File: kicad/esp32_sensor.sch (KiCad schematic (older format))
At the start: 0 parts

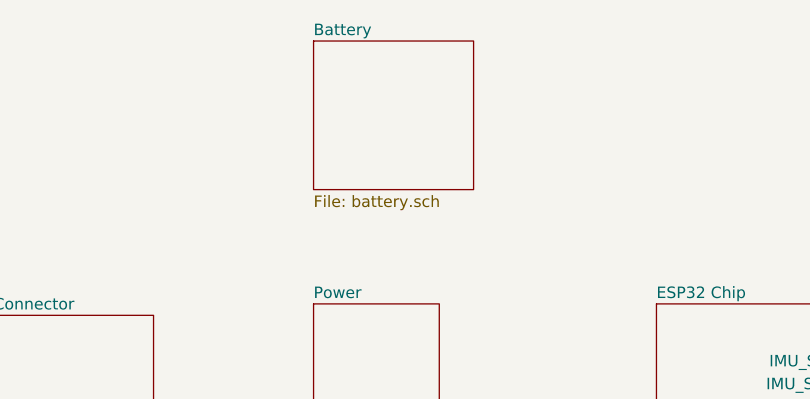
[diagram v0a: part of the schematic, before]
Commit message: Deleted a header pin. Started working on PCB
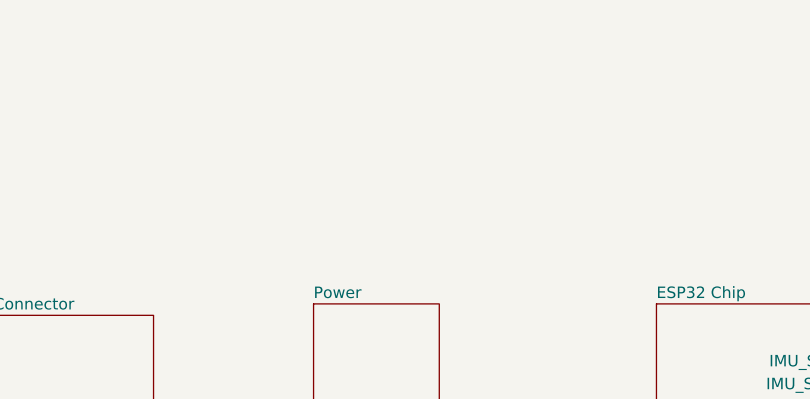
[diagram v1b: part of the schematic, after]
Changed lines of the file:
@@
 $Descr USLetter 11000 8500
 encoding utf-8
-Sheet 1 6
+Sheet 1 5
 Title "ESP32 Sensor Module"
 Date "2020-11-23"
@@
 	6500 3450 5800 3450
 $Sheet
-S 3450 1300 700  650
-U 5FE12D18
-F0 "Battery" 50
-F1 "battery.sch" 50
-$EndSheet
-$Sheet
 S 2050 2500 700  1200

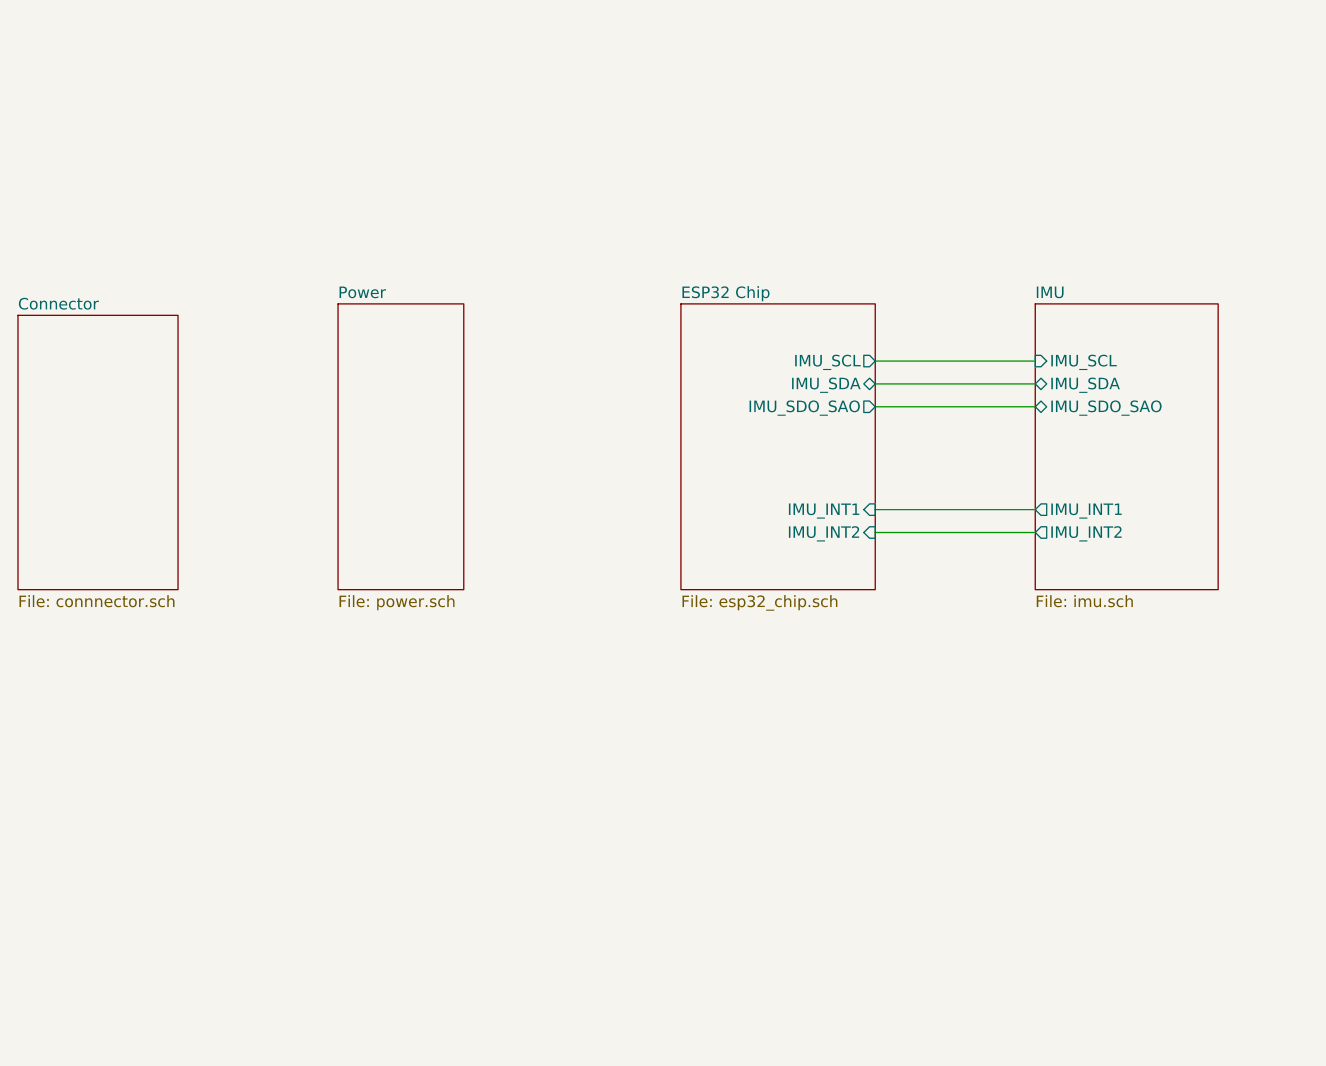
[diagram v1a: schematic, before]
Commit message: Updated schematic and PCB design to v0.0.2 for 2-layer pcb. Added more silkscreen text
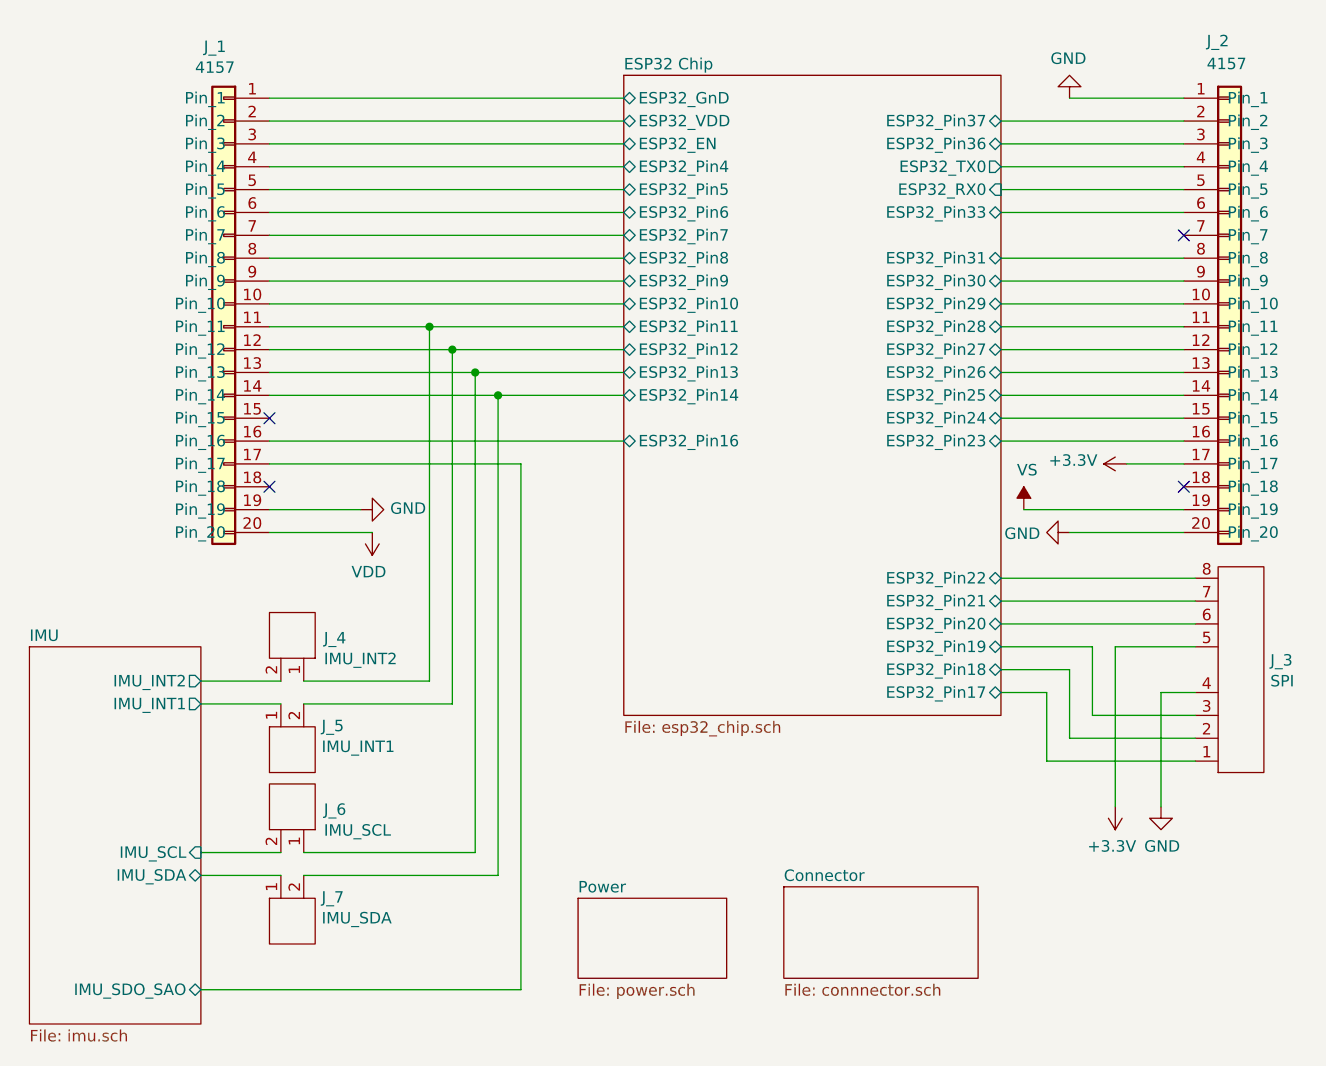
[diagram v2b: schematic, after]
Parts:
- added J_1, J_2: 4157, Connector_PinSocket_2.54mm:PinSocket_1x20_P2.54mm_Vertical, symbol CANtech:4157
- added J_3: SPI, Connector_PinHeader_2.54mm:PinHeader_1x08_P2.54mm_Vertical, symbol CANtech:Header_Pin_8
- added J_4: IMU_INT2, Connector_PinHeader_2.54mm:PinHeader_1x02_P2.54mm_Vertical, symbol CANtech:Header_Pin_2
- added J_5: IMU_INT1, Connector_PinHeader_2.54mm:PinHeader_1x02_P2.54mm_Vertical, symbol CANtech:Header_Pin_2
- added J_6: IMU_SCL, Connector_PinHeader_2.54mm:PinHeader_1x02_P2.54mm_Vertical, symbol CANtech:Header_Pin_2
- added J_7: IMU_SDA, Connector_PinHeader_2.54mm:PinHeader_1x02_P2.54mm_Vertical, symbol CANtech:Header_Pin_2
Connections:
- new net +3V3: J_2.17 (Pin_17), J_3.5
- new net ESP32 Chip/ESP32_EN: J_1.3 (Pin_3)
- new net ESP32 Chip/ESP32_GnD: J_1.1 (Pin_1)
- new net ESP32 Chip/ESP32_Pin10: J_1.10 (Pin_10)
- new net ESP32 Chip/ESP32_Pin11: J_1.11 (Pin_11), J_4.1
- new net ESP32 Chip/ESP32_Pin12: J_1.12 (Pin_12), J_5.2
- new net ESP32 Chip/ESP32_Pin13: J_1.13 (Pin_13), J_6.1
- new net ESP32 Chip/ESP32_Pin14: J_1.14 (Pin_14), J_7.2
- new net ESP32 Chip/ESP32_Pin16: J_1.16 (Pin_16)
- new net ESP32 Chip/ESP32_Pin17: J_3.1
- new net ESP32 Chip/ESP32_Pin18: J_3.2
- new net ESP32 Chip/ESP32_Pin19: J_3.3
- new net ESP32 Chip/ESP32_Pin20: J_3.6
- new net ESP32 Chip/ESP32_Pin21: J_3.7
- new net ESP32 Chip/ESP32_Pin22: J_3.8
- new net ESP32 Chip/ESP32_Pin23: J_2.16 (Pin_16)
- new net ESP32 Chip/ESP32_Pin24: J_2.15 (Pin_15)
- new net ESP32 Chip/ESP32_Pin25: J_2.14 (Pin_14)
- new net ESP32 Chip/ESP32_Pin26: J_2.13 (Pin_13)
- new net ESP32 Chip/ESP32_Pin27: J_2.12 (Pin_12)
- new net ESP32 Chip/ESP32_Pin28: J_2.11 (Pin_11)
- new net ESP32 Chip/ESP32_Pin29: J_2.10 (Pin_10)
- new net ESP32 Chip/ESP32_Pin30: J_2.9 (Pin_9)
- new net ESP32 Chip/ESP32_Pin31: J_2.8 (Pin_8)
- new net ESP32 Chip/ESP32_Pin33: J_2.6 (Pin_6)
- new net ESP32 Chip/ESP32_Pin36: J_2.3 (Pin_3)
- new net ESP32 Chip/ESP32_Pin37: J_2.2 (Pin_2)
- new net ESP32 Chip/ESP32_Pin4: J_1.4 (Pin_4)
- new net ESP32 Chip/ESP32_Pin5: J_1.5 (Pin_5)
- new net ESP32 Chip/ESP32_Pin6: J_1.6 (Pin_6)
- new net ESP32 Chip/ESP32_Pin7: J_1.7 (Pin_7)
- new net ESP32 Chip/ESP32_Pin8: J_1.8 (Pin_8)
- new net ESP32 Chip/ESP32_Pin9: J_1.9 (Pin_9)
- new net ESP32 Chip/ESP32_RX0: J_2.5 (Pin_5)
- new net ESP32 Chip/ESP32_TX0: J_2.4 (Pin_4)
- new net ESP32 Chip/ESP32_VDD: J_1.2 (Pin_2)
- new net GND: J_1.19 (Pin_19), J_2.1 (Pin_1), J_2.20 (Pin_20), J_3.4
- new net IMU/IMU_INT1: J_5.1
- new net IMU/IMU_INT2: J_4.2
- new net IMU/IMU_SCL: J_6.2
- new net IMU/IMU_SDA: J_7.1
- new net IMU/IMU_SDO_SAO: J_1.17 (Pin_17)
- new net VDD: J_1.20 (Pin_20)
- new net VS: J_2.19 (Pin_19)
- no-connect marks 0 -> 4
